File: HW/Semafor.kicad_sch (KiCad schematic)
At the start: 35 parts, among them J1 USB_C_Receptacle_USB2.0, Q1 Q_NMOS_GSD, SW6 SW_SPDT, U1 ESP32-C3, U2 CN3058E, U3 LT1930

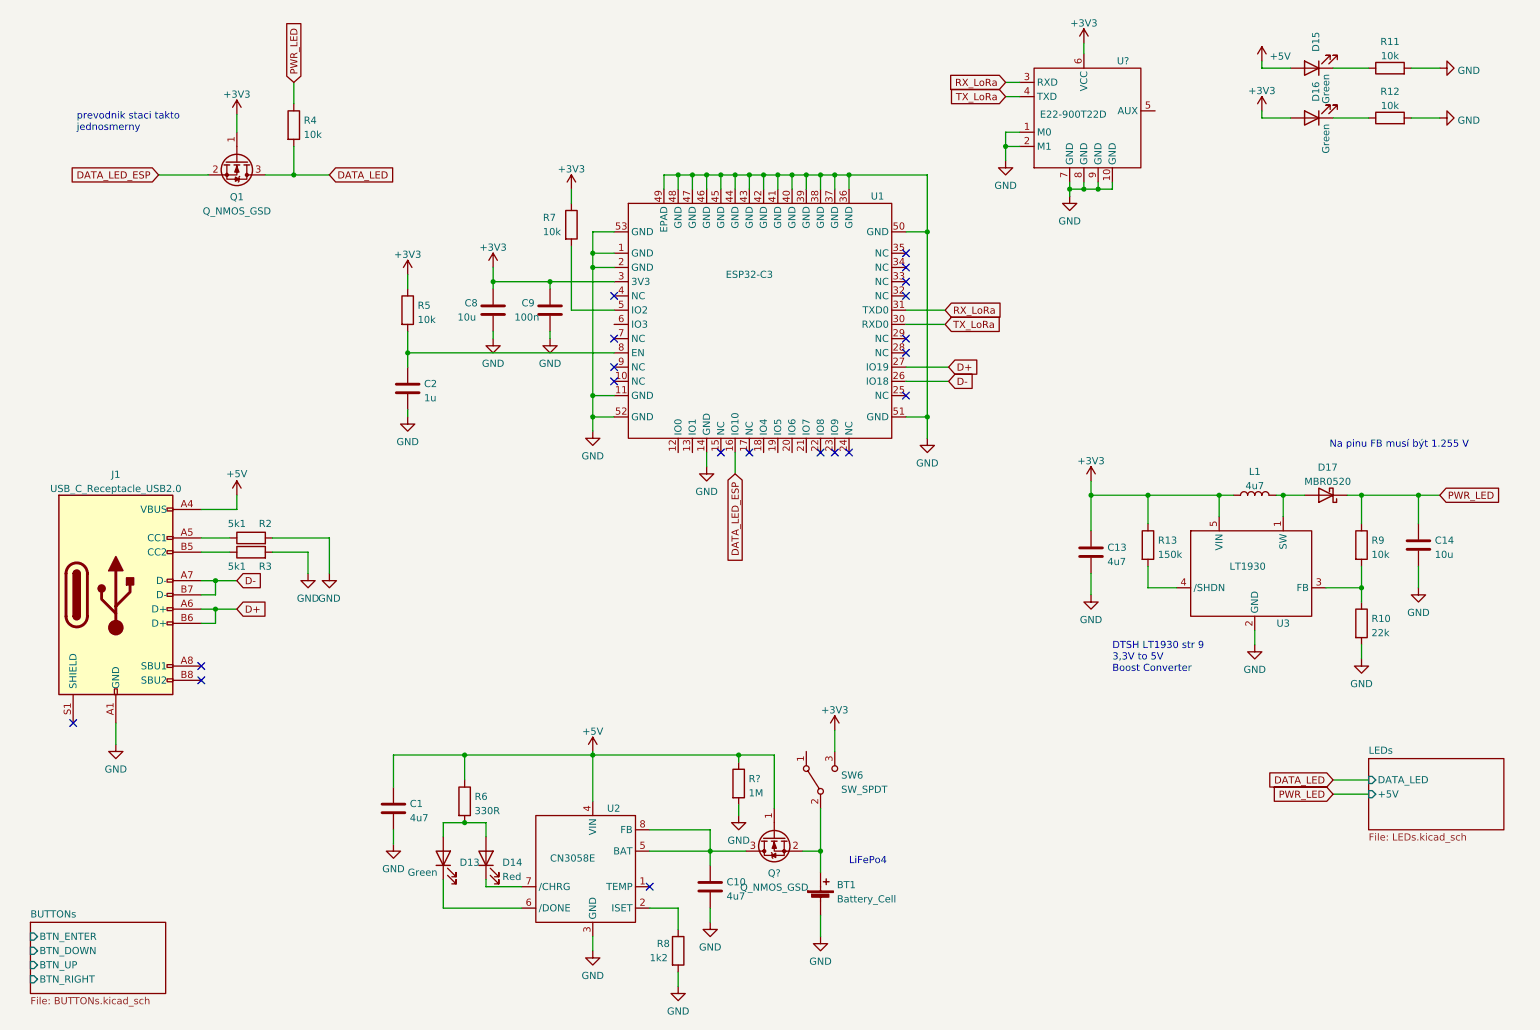
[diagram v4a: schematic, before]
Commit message: update symbol ESP32-C3, add capacitors to WS2812C, add transils to USB
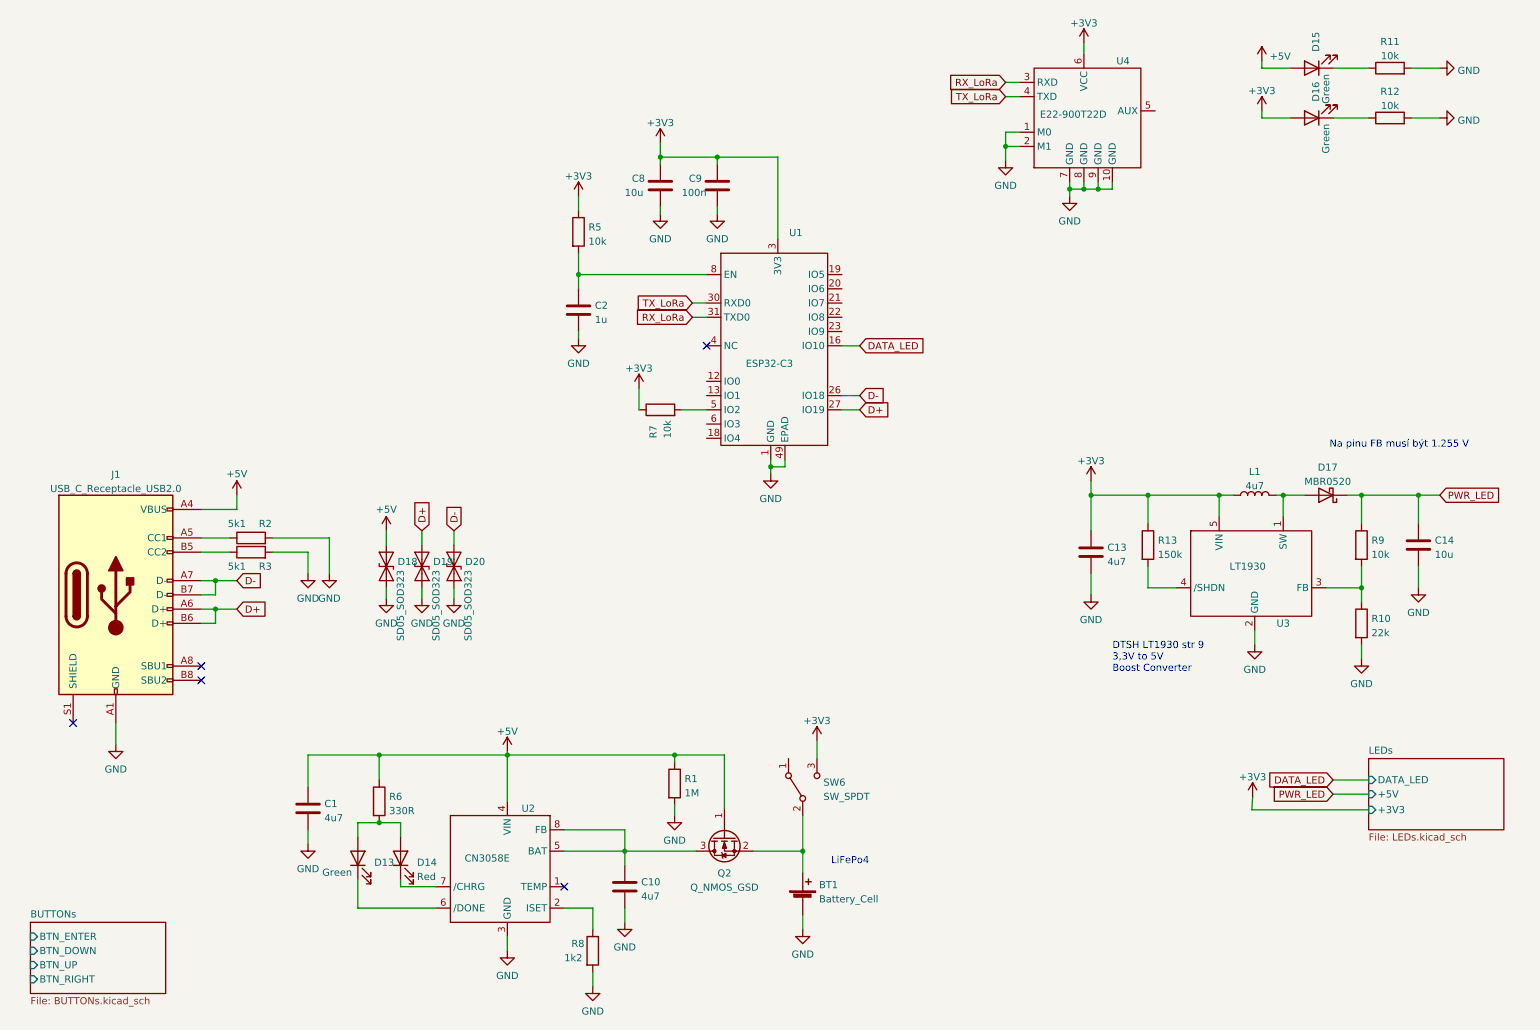
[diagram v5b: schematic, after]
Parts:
- removed Q1: Q_NMOS_GSD, Package_TO_SOT_SMD:SOT-23, symbol Device:Q_NMOS_GSD
- removed R4: 10k, Resistor_SMD:R_0603_1608Metric, symbol Device:R
- added D18, D19, D20: SD05_SOD323, Diode_SMD:D_SOD-323, symbol Diode:SD05_SOD323
- U4: renamed from U?; footprint (none) -> Library:E22-900T22D
- gave numbers to parts that had none: 2
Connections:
- net DATA_LED_ESP is gone; now on net DATA_LED: U1.16 (IO10)
- net +5V: now also D18.2 (A2)
- net D+: now also D19.2 (A2)
- net D-: now also D20.2 (A2)
- net GND: now also D18.1 (A1), D19.1 (A1), D20.1 (A1)
- net at U1.10 (NC): now also U1.15 (NC), U1.17 (NC), U1.24 (NC), U1.25 (NC), U1.28 (NC), U1.29 (NC), U1.32 (NC), U1.33 (NC), U1.34 (NC), U1.35 (NC), U1.4 (NC), U1.7 (NC), U1.9 (NC)
- no-connect marks 20 -> 5
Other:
- sheet LEDs ports: added +3V3; removed none
- note removed: "prevodnik staci takto jednosmerny"
- moved on the sheet: BT1, C1, C10, C2, C8, C9, D13, D14, Q2, R1, R5, R6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

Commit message: add piezo, vibration motor
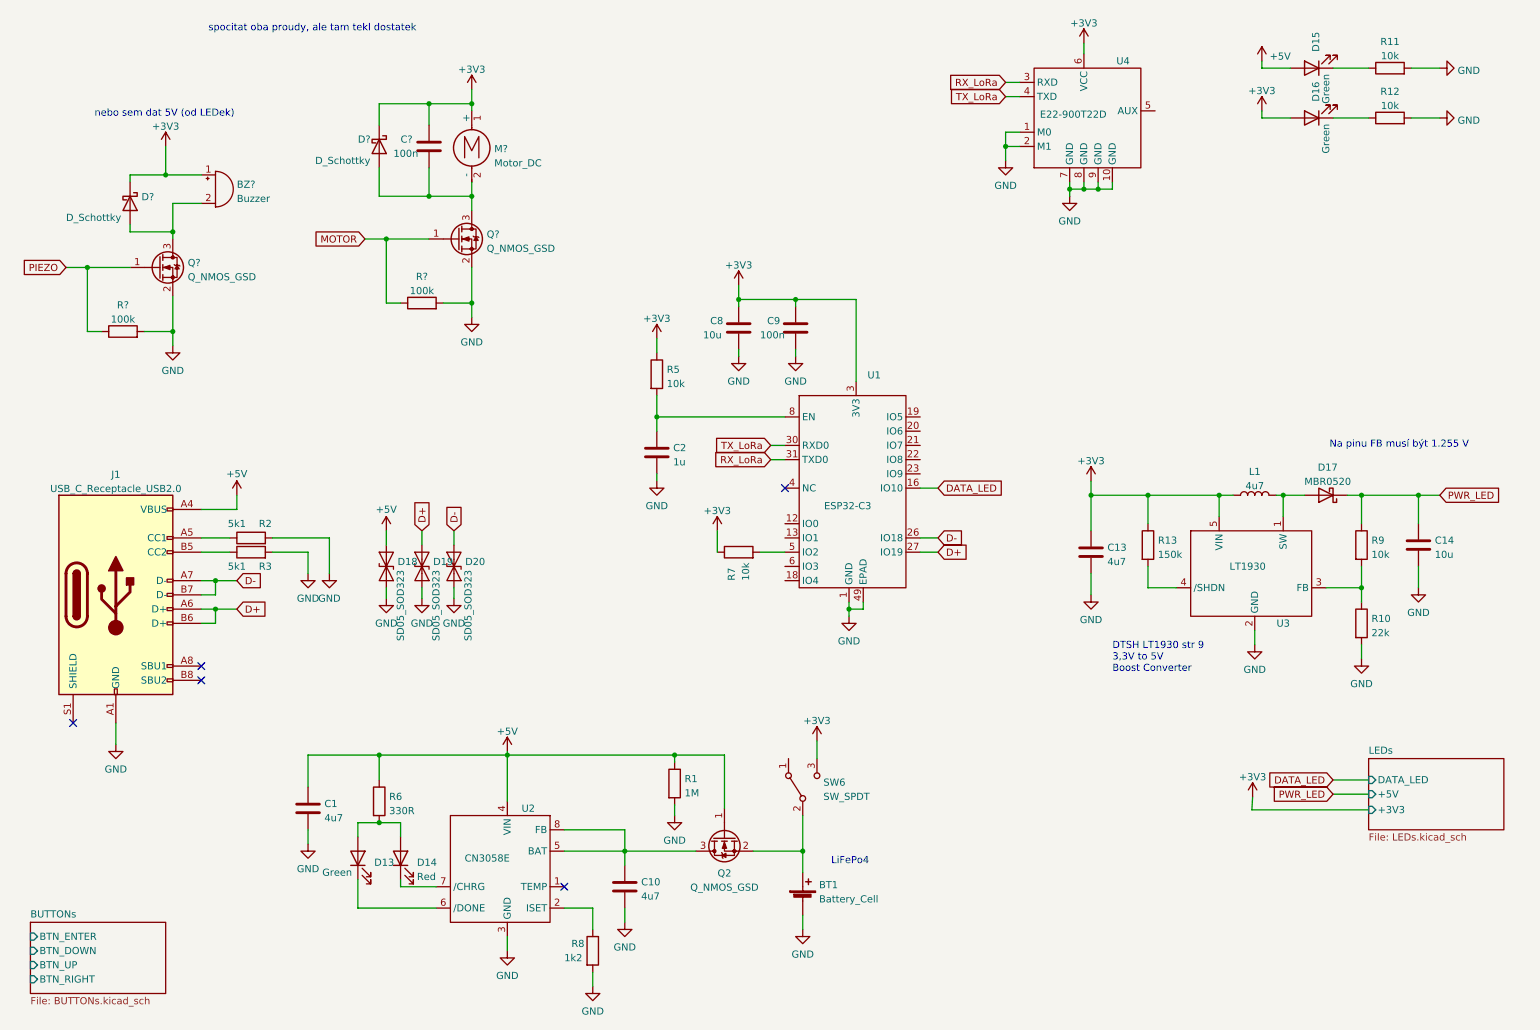
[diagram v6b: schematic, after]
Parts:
- added BZ?: Buzzer, Library:PIEZO, symbol Device:Buzzer
- added C?: 100n, Capacitor_SMD:C_0603_1608Metric, symbol Device:C
- added D? (x2): D_Schottky, Diode_SMD:D_SOD-123, symbol Device:D_Schottky
- added M?: Motor_DC, Connector_PinHeader_2.54mm:PinHeader_1x02_P2.54mm_Vertical, symbol Motor:Motor_DC
- added Q? (x2): Q_NMOS_GSD, Package_TO_SOT_SMD:SOT-23, symbol Device:Q_NMOS_GSD
- added R? (x2): 100k, Resistor_SMD:R_0603_1608Metric, symbol Device:R
- C9: footprint Capacitor_SMD:C_0805_2012Metric -> Capacitor_SMD:C_0603_1608Metric
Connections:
- net +3V3: now also BZ?.1 (-), C?.1, D?.1 (K), D?.1 (K), M?.1 (+)
- net GND: now also Q?.2 (S), Q?.2 (S), R?.2, R?.2
- new net: C?.2, D?.2 (A), M?.2 (-), Q?.3 (D)
- new net: BZ?.2 (+), D?.2 (A), Q?.3 (D)
- new net MOTOR: Q?.1 (G), R?.1
- new net PIEZO: Q?.1 (G), R?.1
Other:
- note added: "nebo sem dat 5V (od LEDek)"
- note added: "spocitat oba proudy, ale tam tekl dostatek"
- moved on the sheet: C2, C8, C9, R5, R7, U1

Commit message: add USB_plug
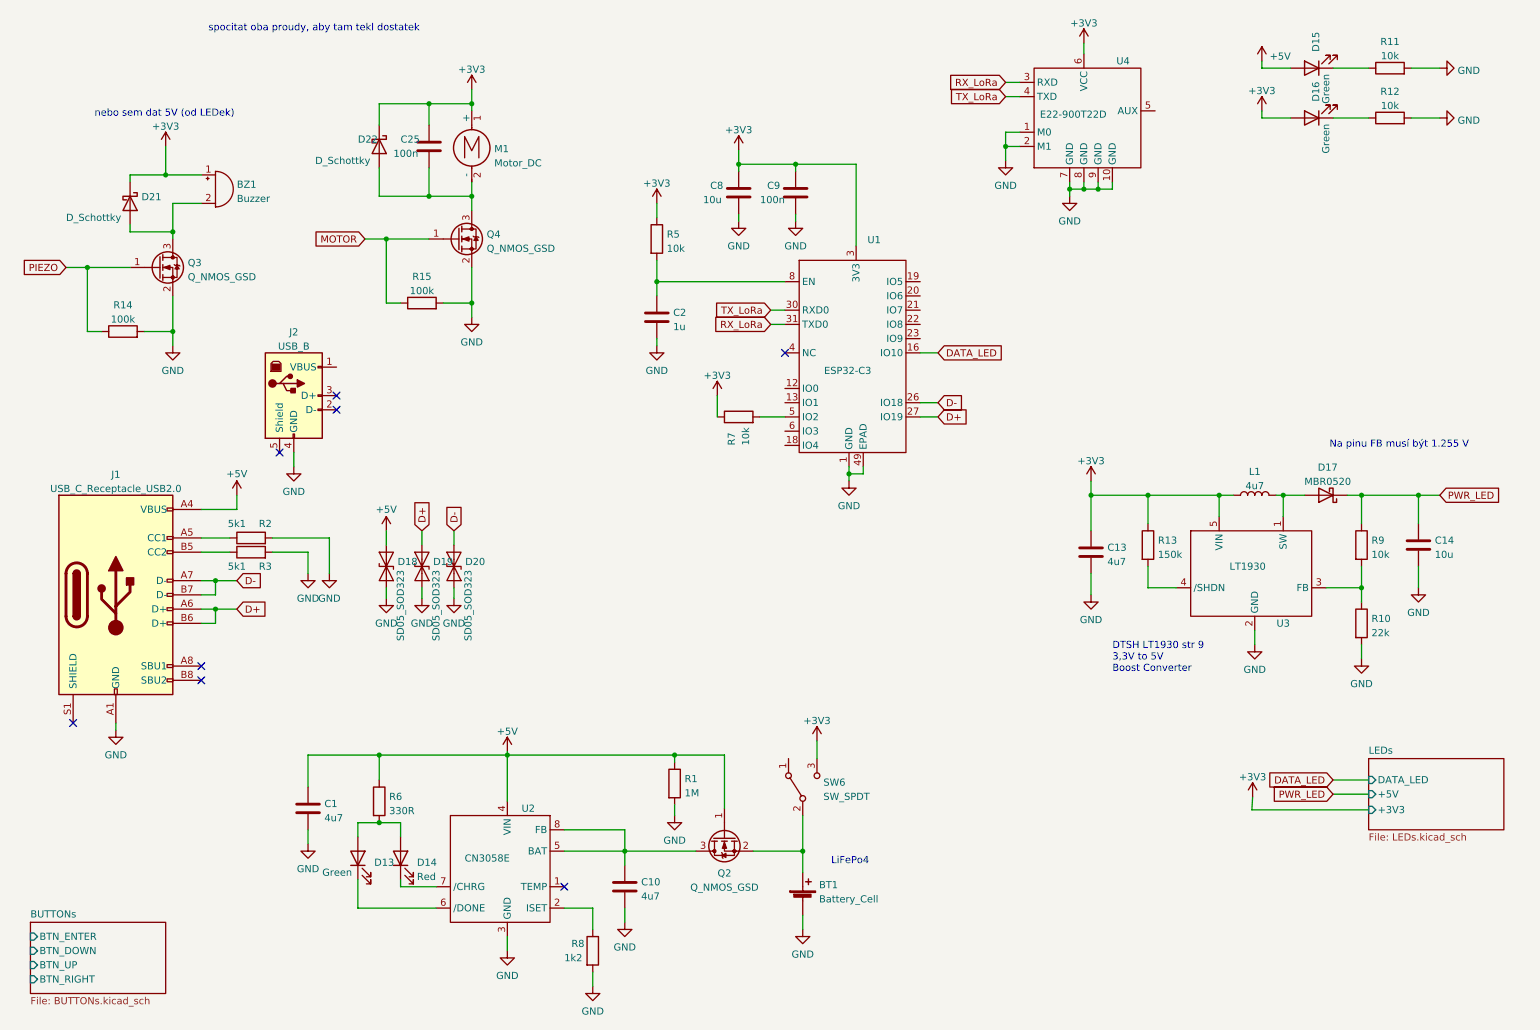
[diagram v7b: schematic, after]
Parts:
- added J2: USB_B, Library:USB_plug, symbol Connector:USB_B
- M1: renamed from M?; LCSC (none) -> C2891560
- gave numbers to parts that had none: 8
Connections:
- net GND: now also J2.4 (GND)
- no-connect marks 5 -> 8
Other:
- note added: "spocitat oba proudy, aby tam tekl dostatek"
- note removed: "spocitat oba proudy, ale tam tekl dostatek"
- moved on the sheet: C2, C8, C9, R5, R7, U1

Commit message: add capacitive touch buttons and converter AT42QT1070
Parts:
- removed J2: USB_B, Library:USB_plug, symbol Connector:USB_B
- added BTN1, BTN2, BTN3, BTN4, BTN5: Cap_btn, Library:Cap_btn, symbol Library:Cap_btn
- added C3: 100u, Capacitor_SMD:C_0805_2012Metric, symbol Device:C
- added C4: 100n, Capacitor_SMD:C_0603_1608Metric, symbol Device:C
- added J2: USB_plug, Library:USB_plug, symbol Library:USB_plug
- added R16, R17, R18, R19, R20, R21, R22, R23: 10k, Resistor_SMD:R_0603_1608Metric, symbol Device:R
- added U5: AT42QT1070-S, Package_SO:SOIC-14_3.9x8.7mm_P1.27mm, symbol Sensor_Touch:AT42QT1070-S
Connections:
- net +3V3: now also C3.1, C4.1, R16.1, R17.1, R18.1, U5.1 (VDD)
- net GND: now also C3.2, C4.2, J2.4 (GND), U5.14 (VSS), U5.2 (MODE)
- new net: BTN3.1, R20.2
- new net: BTN5.1, R21.1
- new net: R21.2, U5.9 (KEY4)
- new net: R16.2, U5.4 (~{RESET})
- new net: BTN1.1, R19.2
- new net: BTN4.1, R23.2
- new net: R19.1, U5.13 (KEY0)
- new net: R23.1, U5.10 (KEY3)
- new net: R20.1, U5.11 (KEY2)
- new net: R22.1, U5.12 (KEY1)
- new net: BTN2.1, R22.2
- new net SCL: R18.2, U5.6 (SCL/OUT3)
- new net SDA: R17.2, U5.3 (SDA/OUT0)
- no-connect marks 8 -> 10
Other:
- removed sheet BUTTONs
- note added: "?"
- moved on the sheet: C2, C8, C9, R5, R7, U1, U4
